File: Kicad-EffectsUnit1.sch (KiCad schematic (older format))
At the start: 102 parts, among them J101 In7, J102 Doepfer connector, J103 Vin 7-12v, J104 In6, J105 In3, J106 Out10, J107 Out11, J108 Out12, J109 Out13, J110 Power Conn, SW101 SW_DPDT_x2, SW102 SW_SPDT, SW103 Rotary_Encoder_Switch, U101 TL072, U102 TL072

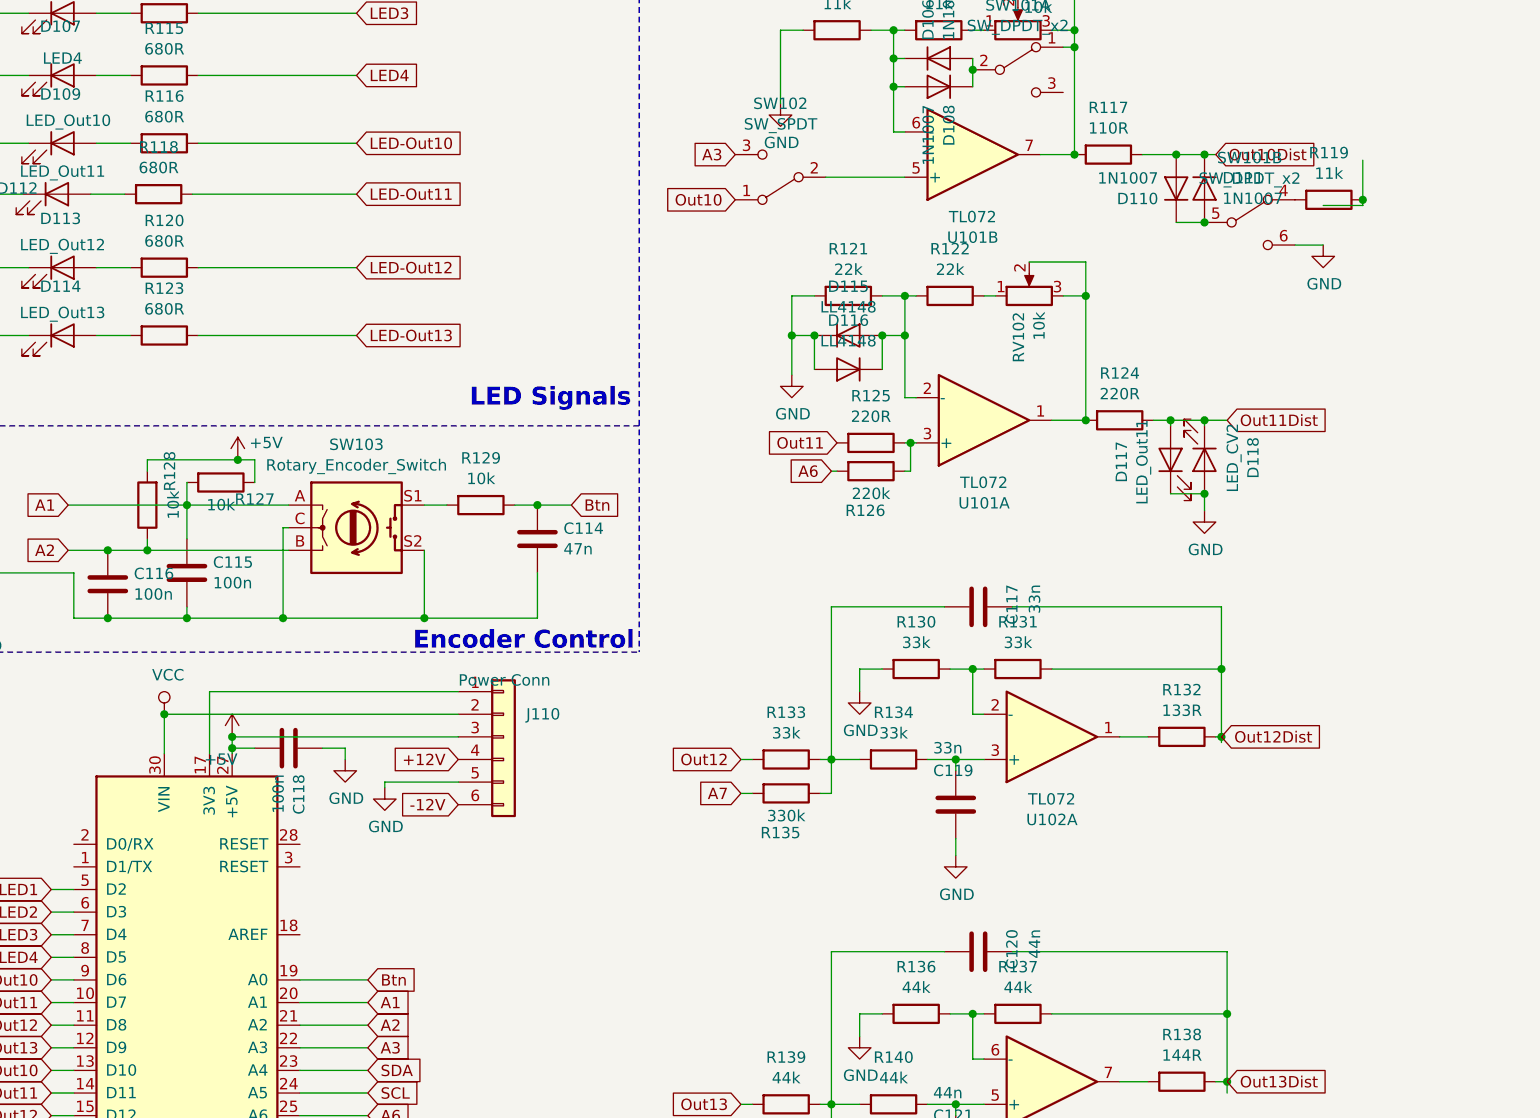
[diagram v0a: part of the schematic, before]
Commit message: Sch added switches and clipping diodes - init pcb
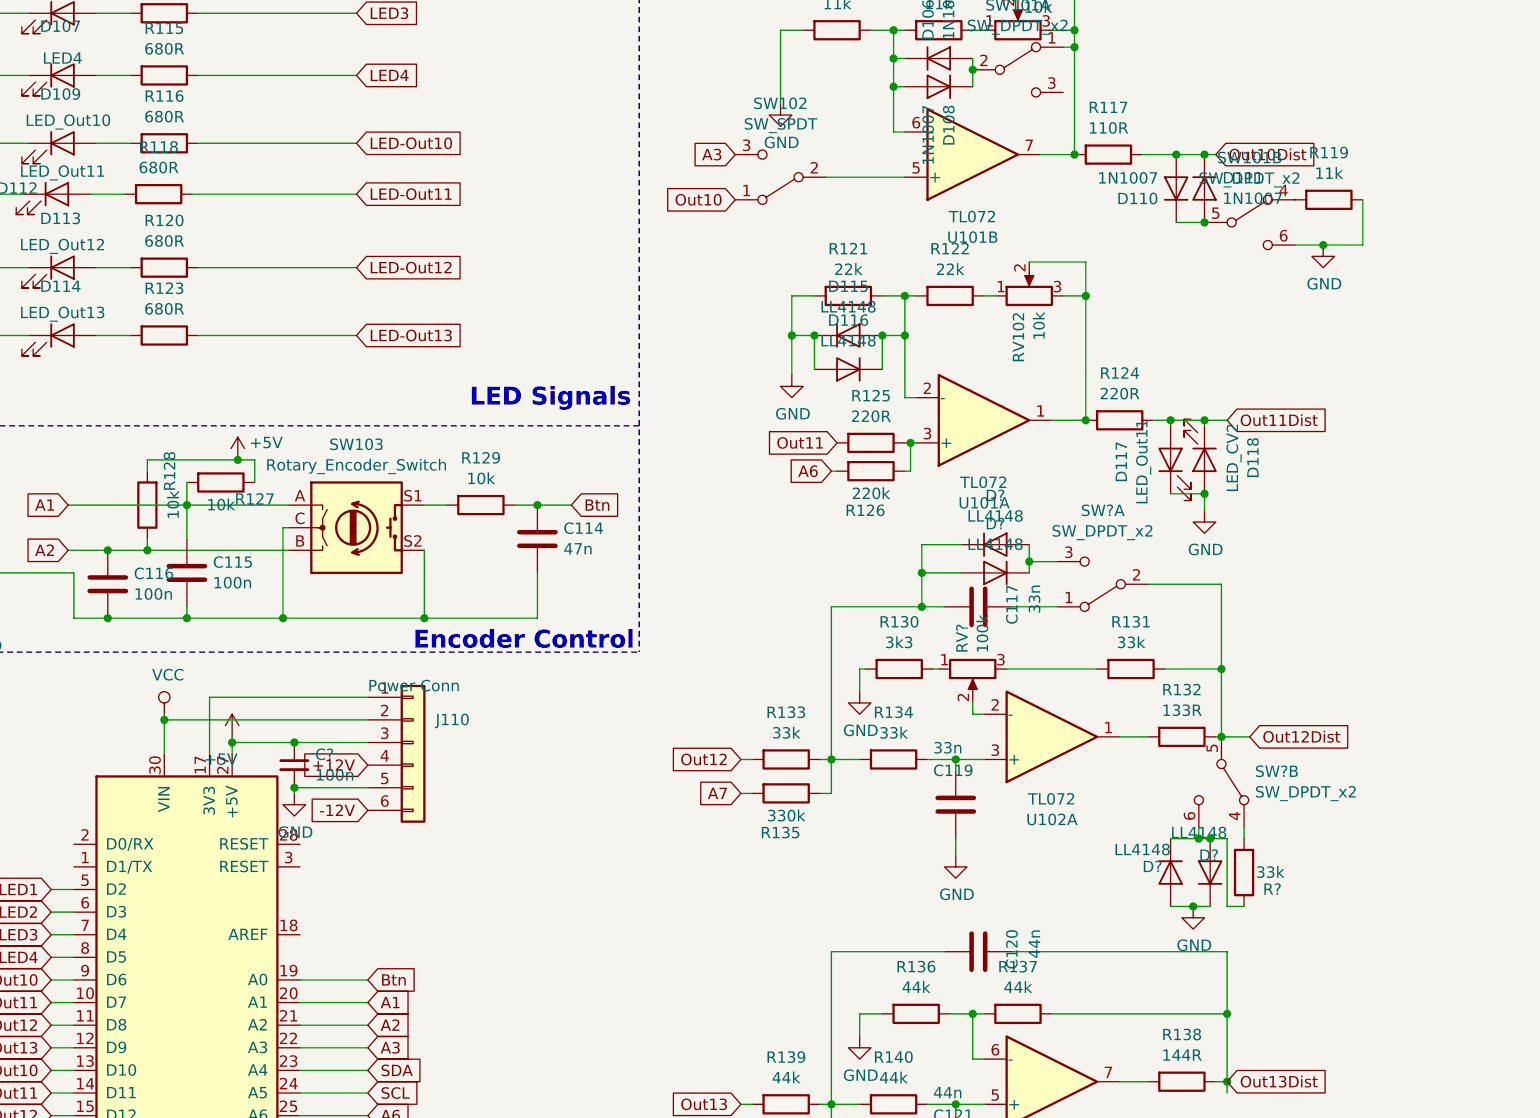
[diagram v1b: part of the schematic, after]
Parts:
- removed C118: 100n, Capacitor_SMD:C_0805_2012Metric_Pad1.15x1.40mm_HandSolder, symbol Device:C
- added C?: 100n, Capacitor_SMD:C_0805_2012Metric_Pad1.15x1.40mm_HandSolder, symbol Device:C_Small
- added D? (x4): LL4148, Diode_SMD:D_MiniMELF, symbol Diode:LL4148
- added R?: 33k, Resistor_SMD:R_0805_2012Metric_Pad1.15x1.40mm_HandSolder, symbol Device:R
- added RV?: 100k, Potentiometer_THT:Potentiometer_Alps_RK09K_Single_Vertical, symbol Device:R_POT
- added SW? (x2): SW_DPDT_x2, AJ-Dropbox-Kicad:SPDTx2, symbol Switch:SW_DPDT_x2
- R130: value 33k -> 3k3
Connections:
- net +5V: now also C?.1
- net GND: now also R119.1, C?.2, D?.1 (K), D?.2 (A)
- net Out12Dist: now also SW?.2 (B), SW?.5 (B); no longer C117.1
- net at C117.2, R133.1, R134.2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: now also D?.1 (K), D?.2 (A)
- new net: RV?.2, U102.2 (-)
- new net: R130.1, RV?.1
- new net: R131.2, RV?.3
- new net: C117.1, SW?.1 (A)
- new net: D?.1 (K), D?.2 (A), SW?.3 (C)
- new net: R?.2, SW?.4 (A)
- new net: D?.1 (K), D?.2 (A), R?.1, SW?.6 (C)
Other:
- moved on the sheet: J110, R130, R131

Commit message: PT2399 started
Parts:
- SW101: value SW_DPDT_x2 -> Dist 10
- SW102: value SW_SPDT -> Crush A3
- SW104: renamed from SW?; value SW_DPDT_x2 -> Dist 12
- gave numbers to parts that had none: 7
- renumbered R102 to R101, R104 to R102, R105 to R103, R106 to R104, R107 to R105, R108 to R106, R109 to R107, R110 to R108, R111 to R109, R112 to R110, R113 to R111, R114 to R112, R115 to R113, R116 to R114, R117 to R115, R118 to R116, R119 to R117, R120 to R118, R121 to R119, R122 to R120, R123 to R121, R124 to R122, R125 to R123, R126 to R124, R127 to R125, R128 to R126, R129 to R127, R130 to R128, R131 to R129, R132 to R130, R133 to R131, R134 to R132, R135 to R133, R136 to R135, R137 to R136, R138 to R137, R139 to R138, R140 to R139, R141 to R140

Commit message: more footprints
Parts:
- J101, J104, J105, J108, J109: footprint Connector_Audio:AudioJack3StereoNarrow-PJ-321 -> AJ-Dropbox-Kicad:PJ301SM
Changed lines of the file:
@@
 F 0 "J108" H 10567 3171 50  0000 R CNN
 F 1 "Out12" H 10567 3080 50  0000 R CNN
-F 2 "Connector_Audio:AudioJack3StereoNarrow-PJ-321" H 10800 3100 50  0001 C CNN
+F 2 "AJ-Dropbox-Kicad:PJ301SM" H 10800 3100 50  0001 C CNN
 F 3 "~" H 10800 3100 50  0001 C CNN
 	1    10800 3100
@@
 F 0 "J109" H 10567 3571 50  0000 R CNN
 F 1 "Out13" H 10567 3480 50  0000 R CNN
-F 2 "Connector_Audio:AudioJack3StereoNarrow-PJ-321" H 10800 3500 50  0001 C CNN
+F 2 "AJ-Dropbox-Kicad:PJ301SM" H 10800 3500 50  0001 C CNN
 F 3 "~" H 10800 3500 50  0001 C CNN
 	1    10800 3500
@@
 F 0 "J104" H 10567 1271 50  0000 R CNN
 F 1 "In6" H 10567 1180 50  0000 R CNN
-F 2 "Connector_Audio:AudioJack3StereoNarrow-PJ-321" H 10800 1200 50  0001 C CNN
+F 2 "AJ-Dropbox-Kicad:PJ301SM" H 10800 1200 50  0001 C CNN
 F 3 "~" H 10800 1200 50  0001 C CNN
 F 4 "VC input" H 10800 1200 50  0001 C CNN "Function"
@@
 F 0 "J101" H 10567 821 50  0000 R CNN
 F 1 "In7" H 10567 730 50  0000 R CNN
-F 2 "Connector_Audio:AudioJack3StereoNarrow-PJ-321" H 10800 750 50  0001 C CNN
+F 2 "AJ-Dropbox-Kicad:PJ301SM" H 10800 750 50  0001 C CNN
 F 3 "~" H 10800 750 50  0001 C CNN
 F 4 "VC input" H 10800 750 50  0001 C CNN "Function"
@@
 F 0 "J105" H 10567 1721 50  0000 R CNN
 F 1 "In3" H 10567 1630 50  0000 R CNN
-F 2 "Connector_Audio:AudioJack3StereoNarrow-PJ-321" H 10800 1650 50  0001 C CNN
+F 2 "AJ-Dropbox-Kicad:PJ301SM" H 10800 1650 50  0001 C CNN
 F 3 "~" H 10800 1650 50  0001 C CNN
 F 4 "VC input" H 10800 1650 50  0001 C CNN "Function"

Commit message: footprint juggling
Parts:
- J103: footprint Connector_BarrelJack:BarrelJack_CUI_PJ-063AH_Horizontal -> Connector_BarrelJack:BarrelJack_Horizontal; symbol Connector:Barrel_Jack -> Connector:Barrel_Jack_Switch
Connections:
- net GND: now also J103.3
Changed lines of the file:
@@
 $EndComp
 $Comp
-L Connector:Barrel_Jack J103
+L Connector:Barrel_Jack_Switch J103
 U 1 1 5C22F3A0
 P 875 1050
 F 0 "J103" H 930 1375 50  0000 C CNN
 F 1 "Vin 7-12v" H 930 1284 50  0000 C CNN
-F 2 "Connector_BarrelJack:BarrelJack_CUI_PJ-063AH_Horizontal" H 925 1010 50  0001 C CNN
+F 2 "Connector_BarrelJack:BarrelJack_Horizontal" H 925 1010 50  0001 C CNN
 F 3 "~" H 925 1010 50  0001 C CNN
 	1    875  1050
@@
 F1 "KicadJE-EU1-PT2399_sub.sch" 50
 $EndSheet
+Wire Wire Line
+	1175 1050 1500 1050
+Wire Wire Line
+	1500 1050 1500 1150
+Connection ~ 1500 1150
 $EndSCHEMATC

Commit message: Footprints
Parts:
- RV101: value 10k -> 10k_O10; footprint Potentiometer_THT:Potentiometer_Alps_RK09K_Single_Vertical -> Potentiometer_THT:Potentiometer_China_RK09_Single_Vertical_AJ
- RV102: value 10k -> 10k_O11; footprint Potentiometer_THT:Potentiometer_Alps_RK09K_Single_Vertical -> Potentiometer_THT:Potentiometer_China_RK09_Single_Vertical_AJ
- RV103: value 100k -> 100k_O12; footprint Potentiometer_THT:Potentiometer_Alps_RK09K_Single_Vertical -> Potentiometer_THT:Potentiometer_China_RK09_Single_Vertical_AJ
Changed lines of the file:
@@
 P 5375 3400
 F 0 "RV102" H 5305 3446 50  0000 R CNN
-F 1 "10k" H 5305 3355 50  0000 R CNN
-F 2 "Potentiometer_THT:Potentiometer_Alps_RK09K_Single_Vertical" H 5375 3400 50  0001 C CNN
+F 1 "10k_O11" H 5305 3355 50  0000 R CNN
+F 2 "Potentiometer_THT:Potentiometer_China_RK09_Single_Vertical_AJ" H 5375 3400 50  0001 C CNN
 F 3 "~" H 5375 3400 50  0001 C CNN
 	1    5375 3400
@@
 P 5325 2225
 F 0 "RV101" V 5525 2300 50  0000 R CNN
-F 1 "10k" V 5425 2200 50  0000 R CNN
-F 2 "Potentiometer_THT:Potentiometer_Alps_RK09K_Single_Vertical" H 5325 2225 50  0001 C CNN
+F 1 "10k_O10" V 5425 2200 50  0000 R CNN
+F 2 "Potentiometer_THT:Potentiometer_China_RK09_Single_Vertical_AJ" H 5325 2225 50  0001 C CNN
 F 3 "~" H 5325 2225 50  0001 C CNN
 	1    5325 2225
@@
 U 1 1 5D077A76
 P 5325 2400
-F 0 "SW101" H 5325 2685 50  0000 C CNN
-F 1 "Dist 10" H 5325 2594 50  0000 C CNN
+F 0 "SW101" H 5400 2400 50  0000 C CNN
+F 1 "Dist 10" H 5375 2325 50  0000 C CNN
 F 2 "AJ-Dropbox-Kicad:SPDTx2" H 5325 2400 50  0001 C CNN
 F 3 "~" H 5325 2400 50  0001 C CNN
@@
 P 5125 5050
 F 0 "RV103" H 5055 5096 50  0000 R CNN
-F 1 "100k" H 5055 5005 50  0000 R CNN
-F 2 "Potentiometer_THT:Potentiometer_Alps_RK09K_Single_Vertical" H 5125 5050 50  0001 C CNN
+F 1 "100k_O12" H 5055 5005 50  0000 R CNN
+F 2 "Potentiometer_THT:Potentiometer_China_RK09_Single_Vertical_AJ" H 5125 5050 50  0001 C CNN
 F 3 "~" H 5125 5050 50  0001 C CNN
 	1    5125 5050

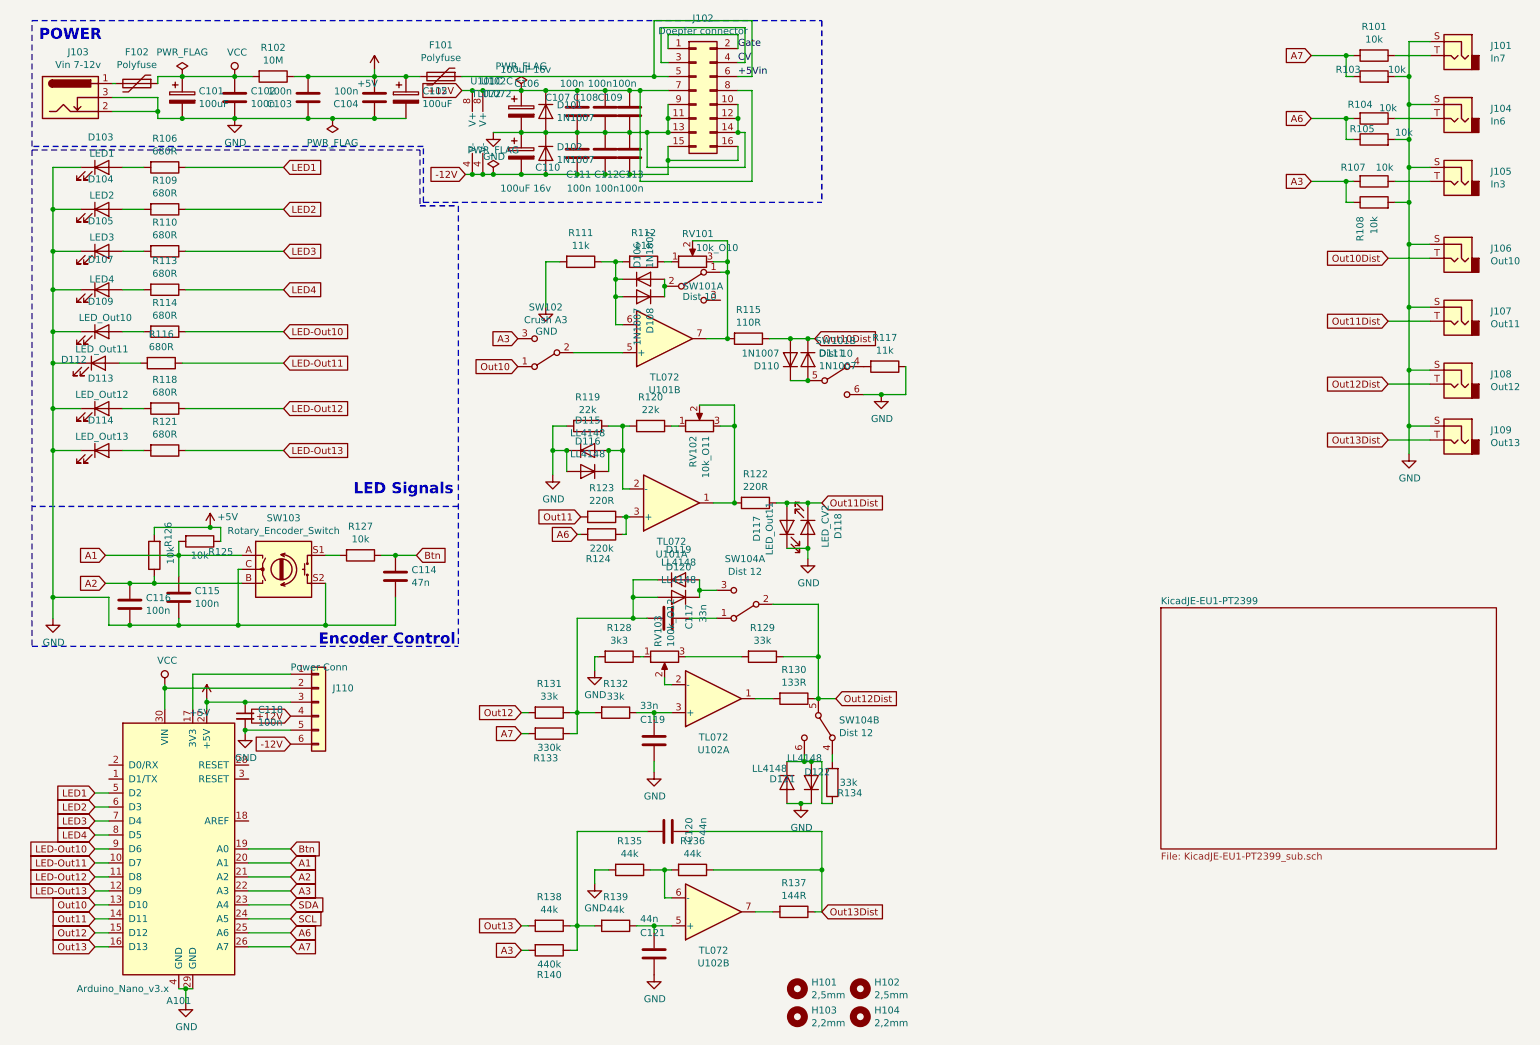
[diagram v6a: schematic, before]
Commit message: Pin juggling on bit crusher
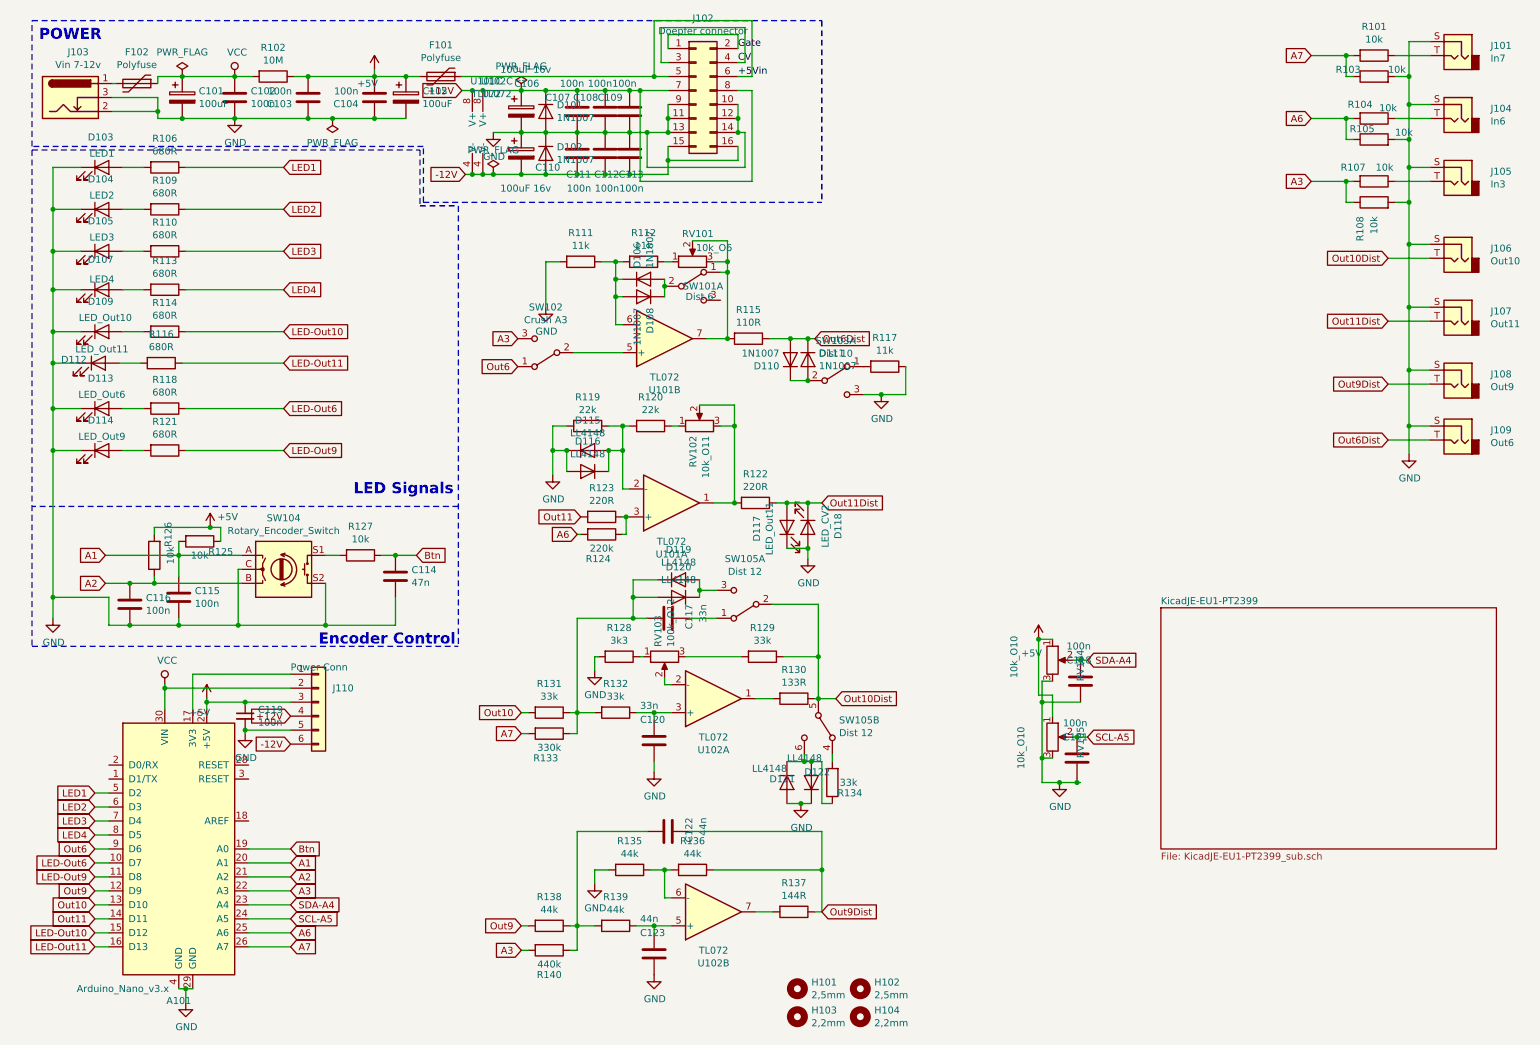
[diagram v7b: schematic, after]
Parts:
- added C118, C121: 100n, Capacitor_SMD:C_0805_2012Metric_Pad1.15x1.40mm_HandSolder, symbol Device:C
- added RV104, RV105: 10k_O10, Potentiometer_THT:Potentiometer_China_RK09_Single_Vertical_AJ, symbol Device:R_POT
- D113: value LED_Out12 -> LED_Out6
- D114: value LED_Out13 -> LED_Out9
- J108: value Out12 -> Out9
- J109: value Out13 -> Out6
- RV101: value 10k_O10 -> 10k_O6
- SW101: value Dist 10 -> Dist 6
- renumbered C118 to C119, C119 to C120, C120 to C122, C121 to C123, SW101 to SW103, SW103 to SW104, SW104 to SW105
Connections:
- net +5V: now also RV104.1, RV105.1
- net GND: now also SW103.3 (C), C118.2, C121.2, RV104.3, RV105.3; no longer SW103.6 (C)
- net LED-Out10: now also A101.15 (D12); no longer A101.9 (D6)
- net LED-Out11: now also A101.16 (D13); no longer A101.10 (D7)
- net Out10: now also R131.2; no longer SW102.1 (A)
- net Out10Dist: now also R129.1, R130.1, SW105.2 (B), SW105.5 (B); no longer D110.2 (A), D111.1 (K), R115.1
- net at D110.1 (K), D111.2 (A): now also SW103.2 (B); no longer SW103.5 (B)
- net at R117.2: now also SW103.1 (A); no longer SW103.4 (A)
- net LED-Out12 renamed LED-Out6
- net LED-Out6: now also A101.10 (D7); no longer A101.11 (D8)
- net LED-Out13 renamed LED-Out9
- net LED-Out9: now also A101.11 (D8); no longer A101.12 (D9)
- removed net Out12: A101.15 (D12), R131.2
- removed net Out12Dist: J108.T, R129.1, R130.1, SW105.2 (B), SW105.5 (B)
- net Out13 renamed Out9
- net Out9: now also A101.12 (D9); no longer A101.16 (D13)
- net Out13Dist renamed Out9Dist
- net Out9Dist: now also J108.T; no longer J109.T
- net SCL renamed SCL-A5
- net SCL-A5: now also C121.1, RV105.2
- net SDA renamed SDA-A4
- net SDA-A4: now also C118.1, RV104.2
- new net Out6: A101.9 (D6), SW102.1 (A)
- new net Out6Dist: D110.2 (A), D111.1 (K), J109.T, R115.1

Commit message: PCB
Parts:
- SW105: value Dist 12 -> Dist 10
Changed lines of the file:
@@
 P 5700 4675
 F 0 "SW105" H 5700 4350 50  0000 C CNN
-F 1 "Dist 12" H 5700 4441 50  0000 C CNN
+F 1 "Dist 10" H 5700 4441 50  0000 C CNN
 F 2 "AJ-Dropbox-Kicad:SPDTx2" H 5700 4675 50  0001 C CNN
 F 3 "~" H 5700 4675 50  0001 C CNN
@@
 P 6225 5550
 F 0 "SW105" V 6179 5698 50  0000 L CNN
-F 1 "Dist 12" V 6270 5698 50  0000 L CNN
+F 1 "Dist 10" V 6270 5698 50  0000 L CNN
 F 2 "AJ-Dropbox-Kicad:SPDTx2" H 6225 5550 50  0001 C CNN
 F 3 "~" H 6225 5550 50  0001 C CNN
